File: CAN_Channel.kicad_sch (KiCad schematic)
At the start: 7 parts, among them J3 Conn_01x01, U2 TJA1051T-3

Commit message: LCD connector, backlight, other work
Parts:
- removed J3: Conn_01x01, Connector_PinHeader_2.54mm:PinHeader_1x01_P2.54mm_Vertical, symbol Connector_Generic:Conn_01x01
- removed S4: SLW-864587-2A-RA-N-D, SamacSys_Parts:SLW8645872ARAND, symbol SamacSys_Parts:SLW-864587-2A-RA-N-D
- added JP3: SolderJumper_2_Open, Jumper:SolderJumper-2_P1.3mm_Open_RoundedPad1.0x1.5mm, symbol Jumper:SolderJumper_2_Open
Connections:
- net CAN-: now also JP3.2 (B)
- net at R6.2: now also JP3.1 (A)
- no-connect marks 3 -> 0
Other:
- moved on the sheet: C15
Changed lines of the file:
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@@
 	(paper "A4")
 	(junction
-		(at 62.23 74.93)
+		(at 74.93 74.93)
 		(diameter 0)
 		(color 0 0 0 0)
@@
 		(color 0 0 0 0)
 	)
-	(no_connect
-		(at 180.34 76.2)
-	)
-	(no_connect
-		(at 180.34 66.04)
-	)
-	(no_connect
-		(at 180.34 68.58)
-	)
 	(wire
 		(pts
@@
 	(wire
 		(pts
-			(xy 62.23 74.93) (xy 93.98 74.93)
-		)
-		(stroke
-			(width 0)
-			(type default)
-		)
-	)
-	(wire
-		(pts
-			(xy 62.23 83.82) (xy 106.68 83.82)
-		)
-		(stroke
-			(width 0)
-			(type default)
-		)
-	)
-	(wire
-		(pts
-			(xy 62.23 74.93) (xy 62.23 72.39)
+			(xy 74.93 74.93) (xy 93.98 74.93)
+		)
+		(stroke
+			(width 0)
+			(type default)
+		)
+	)
+	(wire
+		(pts
+			(xy 74.93 83.82) (xy 106.68 83.82)
+		)
+		(stroke
+			(width 0)
+			(type default)
+		)
+	)
+	(wire
+		(pts
+			(xy 74.93 74.93) (xy 74.93 72.39)
 		)
 		(stroke
@@
 	(wire
 		(pts
-			(xy 62.23 82.55) (xy 62.23 83.82)
-		)
-		(stroke
-			(width 0)
-			(type default)
-		)
-	)
-	(wire
-		(pts
-			(xy 83.82 77.47) (xy 93.98 77.47)
+			(xy 74.93 82.55) (xy 74.93 83.82)
 		)
 		(stroke
@@
 	(hierarchical_label "CAN-"
 		(shape bidirectional)
-		(at 180.34 71.12 180)
+		(at 187.96 73.66 0)
 		(effects
 			(font
 				(size 1.27 1.27)
 			)
-			(justify right)
+			(justify left)
 		)
 	)
@@
 	)
 	(symbol
+		(lib_id "Jumper:SolderJumper_2_Open")
+		(at 184.15 73.66 0)
+		(unit 1)
+		(exclude_from_sim no)
+		(in_bom no)
+		(on_board yes)
+		(dnp no)
+		(fields_autoplaced yes)
+		(property "Reference" "JP3"
+			(at 184.15 67.31 0)
+			(effects
+				(font
+					(size 1.27 1.27)
+				)
+			)
+		)
+		(property "Value" "SolderJumper_2_Open"
+			(at 184.15 69.85 0)
+			(effects
+				(font
+					(size 1.27 1.27)
+				)
+			)
+		)
+		(property "Footprint" "Jumper:SolderJumper-2_P1.3mm_Open_RoundedPad1.0x1.5mm"
+			(at 184.15 73.66 0)
+			(effects
+				(font
+					(size 1.27 1.27)
+				)
+				(hide yes)
+			)
+		)
+		(property "Datasheet" "~"
+			(at 184.15 73.66 0)
+			(effects
+				(font
+					(size 1.27 1.27)
+				)
+				(hide yes)
+			)
+		)
+		(property "Description" "Solder Jumper, 2-pole, open"
+			(at 184.15 73.66 0)
+			(effects
+				(font
+					(size 1.27 1.27)
+				)
+				(hide yes)
+			)
+		)
+		(pin "2"
+		)
+		(pin "1"
+		)
+		(instances
+			(project "LV3-Dash"
+				(path "/f2bb7816-6b2a-47fd-8906-eb4aedd6f9e6/61479cd4-0d84-48d3-a2a5-35c815fbc6c8/26a5cdba-a2c0-4c6f-9b9d-6ff8cc92f2cc"
+					(reference "JP3")
+					(unit 1)
+				)
+			)
+		)
+	)
+	(symbol
 		(lib_id "power:+3.3V")
-		(at 62.23 72.39 0)
+		(at 74.93 72.39 0)
 		(unit 1)
 		(exclude_from_sim no)
@@
 		(fields_autoplaced yes)
 		(property "Reference" "#PWR019"
-			(at 62.23 76.2 0)
+			(at 74.93 76.2 0)
 			(effects
 				(font
@@
 		)
 		(property "Value" "+3.3V"
-			(at 62.23 67.31 0)
+			(at 74.93 67.31 0)
 			(effects
 				(font
@@
 		)
 		(property "Footprint" ""
-			(at 62.23 72.39 0)
+			(at 74.93 72.39 0)
 			(effects
 				(font
@@
 		)
 		(property "Datasheet" ""
-			(at 62.23 72.39 0)
+			(at 74.93 72.39 0)
 			(effects
 				(font
@@
 		)
 		(property "Description" "Power symbol creates a global label with name \"+3.3V\""
-			(at 62.23 72.39 0)
+			(at 74.93 72.39 0)
 			(effects
 				(font
@@
 	)
 	(symbol
-		(lib_id "Connector_Generic:Conn_01x01")
-		(at 78.74 77.47 180)
-		(unit 1)
-		(exclude_from_sim no)
-		(in_bom yes)
-		(on_board yes)
-		(dnp no)
-		(fields_autoplaced yes)
-		(property "Reference" "J3"
-			(at 78.74 71.12 0)
-			(effects
-				(font
-					(size 1.27 1.27)
-				)
-			)
-		)
-		(property "Value" "Conn_01x01"
-			(at 78.74 73.66 0)
-			(effects
-				(font
-					(size 1.27 1.27)
-				)
-			)
-		)
-		(property "Footprint" "Connector_PinHeader_2.54mm:PinHeader_1x01_P2.54mm_Vertical"
-			(at 78.74 77.47 0)
-			(effects
-				(font
-					(size 1.27 1.27)
-				)
-				(hide yes)
-			)
-		)
-		(property "Datasheet" "~"
-			(at 78.74 77.47 0)
-			(effects
-				(font
-					(size 1.27 1.27)
-				)
-				(hide yes)
-			)
-		)
-		(property "Description" "Generic connector, single row, 01x01, script generated (kicad-library-utils/schlib/autogen/connector/)"
-			(at 78.74 77.47 0)
-			(effects
-				(font
-					(size 1.27 1.27)
-				)
-				(hide yes)
-			)
-		)
-		(pin "1"
-		)
-		(instances
-			(project "LV3-Core"
-				(path "/f2bb7816-6b2a-47fd-8906-eb4aedd6f9e6/61479cd4-0d84-48d3-a2a5-35c815fbc6c8/26a5cdba-a2c0-4c6f-9b9d-6ff8cc92f2cc"
-					(reference "J3")
-					(unit 1)
-				)
-			)
-		)
-	)
-	(symbol
 		(lib_id "power:GND")
 		(at 106.68 83.82 0)
@@
 	(symbol
 		(lib_id "Device:C")
-		(at 62.23 78.74 0)
+		(at 74.93 78.74 0)
 		(unit 1)
 		(exclude_from_sim no)
@@
 		(fields_autoplaced yes)
 		(property "Reference" "C15"
-			(at 66.04 77.4699 0)
+			(at 78.74 77.4699 0)
 			(effects
 				(font
@@
 		)
 		(property "Value" "100n"
-			(at 66.04 80.0099 0)
+			(at 78.74 80.0099 0)
 			(effects
 				(font
@@
 		)
 		(property "Footprint" "Capacitor_SMD:C_0603_1608Metric_Pad1.08x0.95mm_HandSolder"
-			(at 63.1952 82.55 0)
+			(at 75.8952 82.55 0)
 			(effects
 				(font
@@
 		)
 		(property "Datasheet" "~"
-			(at 62.23 78.74 0)
+			(at 74.93 78.74 0)
 			(effects
 				(font
@@
 		)
 		(property "Description" "Unpolarized capacitor"
-			(at 62.23 78.74 0)
+			(at 74.93 78.74 0)
 			(effects
 				(font
@@
 					(unit 1)
 				)
-			)
-		)
-	)
-	(symbol
-		(lib_id "SamacSys_Parts:SLW-864587-2A-RA-N-D")
-		(at 180.34 66.04 0)
-		(unit 1)
-		(exclude_from_sim no)
-		(in_bom yes)
-		(on_board yes)
-		(dnp no)
-		(fields_autoplaced yes)
-		(property "Reference" "S4"
-			(at 199.39 69.8499 0)
-			(effects
-				(font
-					(size 1.27 1.27)
-				)
-				(justify left)
-			)
-		)
-		(property "Value" "SLW-864587-2A-RA-N-D"
-			(at 199.39 72.3899 0)
-			(effects
-				(font
-					(size 1.27 1.27)
-				)
-				(justify left)
-			)
-		)
-		(property "Footprint" "SamacSys_Parts:SLW8645872ARAND"
-			(at 199.39 160.96 0)
-			(effects
-				(font
-					(size 1.27 1.27)
-				)
-				(justify left top)
-				(hide yes)
-			)
-		)
-		(property "Datasheet" "https://www.sameskydevices.com/product/resource/slw-864587-2a-ra-n-d.pdf"
-			(at 199.39 260.96 0)
-			(effects
-				(font
-					(size 1.27 1.27)
-				)
-				(justify left top)
-				(hide yes)
-			)
-		)
-		(property "Description" "8.6 x 4.5 x 8.7 mm, 2 mm Raised Slide Actuator, Right Angle, Through Hole, Slide Switch"
-			(at 180.34 66.04 0)
-			(effects
-				(font
-					(size 1.27 1.27)
-				)
-				(hide yes)
-			)
-		)
-		(property "Height" "6.3"
-			(at 199.39 460.96 0)
-			(effects
-				(font
-					(size 1.27 1.27)
-				)
-				(justify left top)
-				(hide yes)
-			)
-		)
-		(property "Mouser Part Number" "179-SLW8645872ARAND"
-			(at 199.39 560.96 0)
-			(effects
-				(font
-					(size 1.27 1.27)
-				)
-				(justify left top)
-				(hide yes)
-			)
-		)
-		(property "Mouser Price/Stock" "https://www.mouser.co.uk/ProductDetail/Same-Sky/SLW-864587-2A-RA-N-D?qs=IKkN%2F947nfDwxE1B2lS5tw%3D%3D"
-			(at 199.39 660.96 0)
-			(effects
-				(font
-					(size 1.27 1.27)
-				)
-				(justify left top)
-				(hide yes)
-			)
-		)
-		(property "Manufacturer_Name" "Same Sky"
-			(at 199.39 760.96 0)
-			(effects
-				(font
-					(size 1.27 1.27)
-				)
-				(justify left top)
-				(hide yes)
-			)
-		)
-		(property "Manufacturer_Part_Number" "SLW-864587-2A-RA-N-D"
-			(at 199.39 860.96 0)
-			(effects
-				(font
-					(size 1.27 1.27)
-				)
-				(justify left top)
-				(hide yes)
-			)
-		)
-		(pin "2"
-		)
-		(pin "4"
-		)
-		(pin "5"
-		)
-		(pin "1"
-		)
-		(pin "3"
-		)
-		(instances
-			(project "LV3-Core"
-				(path "/f2bb7816-6b2a-47fd-8906-eb4aedd6f9e6/61479cd4-0d84-48d3-a2a5-35c815fbc6c8/26a5cdba-a2c0-4c6f-9b9d-6ff8cc92f2cc"
-					(reference "S4")
-					(unit 1)
-				)

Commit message: preliminary complete schematic
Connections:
- net GND: now also U2.8 (S)
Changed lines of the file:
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@@
+	)
+	(junction
+		(at 90.17 83.82)
+		(diameter 0)
+		(color 0 0 0 0)
 	)
 	(junction
@@
 		(pts
 			(xy 165.1 73.66) (xy 162.56 73.66)
+		)
+		(stroke
+			(width 0)
+			(type default)
+		)
+	)
+	(wire
+		(pts
+			(xy 90.17 77.47) (xy 90.17 83.82)
+		)
+		(stroke
+			(width 0)
+			(type default)
+		)
+	)
+	(wire
+		(pts
+			(xy 93.98 77.47) (xy 90.17 77.47)
+		)
+		(stroke
+			(width 0)
+			(type default)
+		)
+	)
+	(wire
+		(pts
+			(xy 90.17 83.82) (xy 106.68 83.82)
 		)
 		(stroke
@@
 	(wire
 		(pts
-			(xy 74.93 83.82) (xy 106.68 83.82)
+			(xy 74.93 83.82) (xy 90.17 83.82)
 		)
 		(stroke

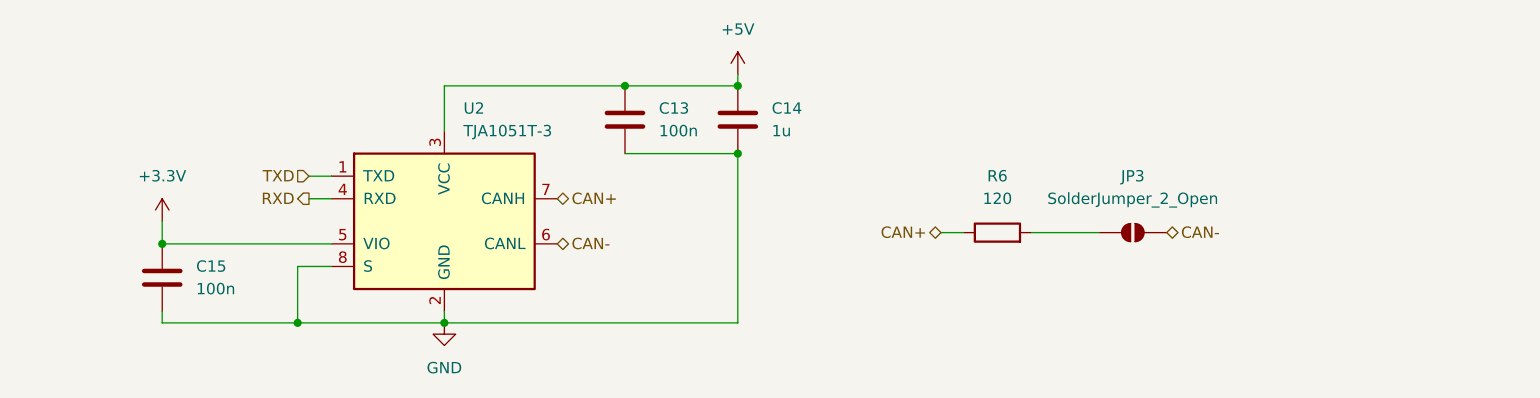
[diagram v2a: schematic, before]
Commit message: basic layout organization, fix +VDDA typo
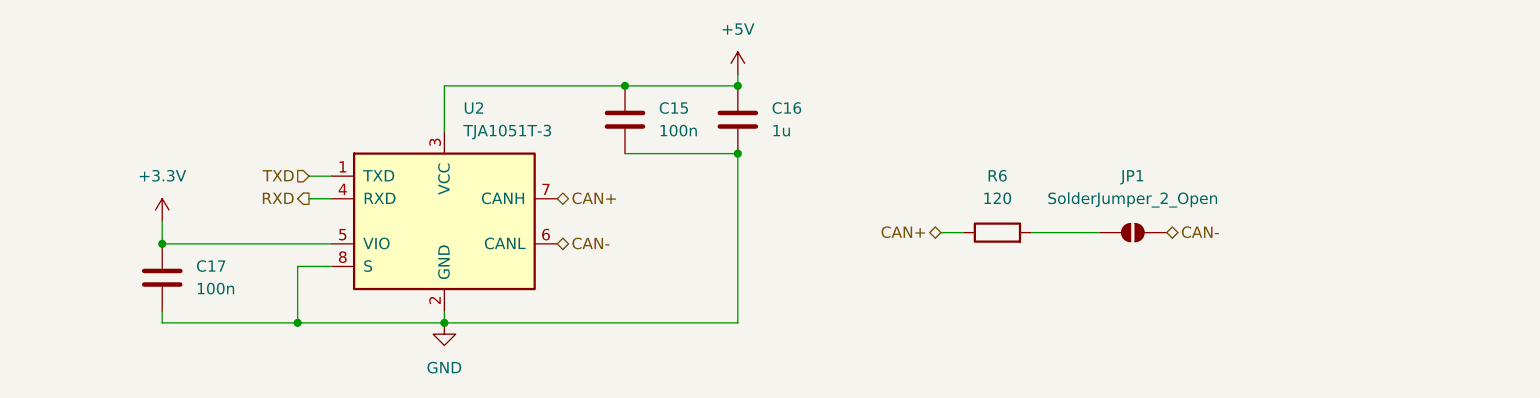
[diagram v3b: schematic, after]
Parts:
- renumbered C13 to C15, C14 to C16, C15 to C17, JP3 to JP1
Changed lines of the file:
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@@
 		(dnp no)
 		(fields_autoplaced yes)
-		(property "Reference" "JP3"
+		(property "Reference" "JP1"
 			(at 184.15 67.31 0)
 			(effects
@@
 			(project "LV3-Dash"
 				(path "/f2bb7816-6b2a-47fd-8906-eb4aedd6f9e6/61479cd4-0d84-48d3-a2a5-35c815fbc6c8/26a5cdba-a2c0-4c6f-9b9d-6ff8cc92f2cc"
-					(reference "JP3")
+					(reference "JP1")
 					(unit 1)
 				)
@@
 		(dnp no)
 		(fields_autoplaced yes)
-		(property "Reference" "#PWR019"
+		(property "Reference" "#PWR020"
 			(at 74.93 76.2 0)
 			(effects
@@
 			(project "LV3-Core"
 				(path "/f2bb7816-6b2a-47fd-8906-eb4aedd6f9e6/61479cd4-0d84-48d3-a2a5-35c815fbc6c8/26a5cdba-a2c0-4c6f-9b9d-6ff8cc92f2cc"
-					(reference "#PWR019")
+					(reference "#PWR020")
 					(unit 1)
 				)
@@
 		(dnp no)
 		(fields_autoplaced yes)
-		(property "Reference" "#PWR018"
+		(property "Reference" "#PWR019"
 			(at 139.7 59.69 0)
 			(effects
@@
 			(project "LV3-Core"
 				(path "/f2bb7816-6b2a-47fd-8906-eb4aedd6f9e6/61479cd4-0d84-48d3-a2a5-35c815fbc6c8/26a5cdba-a2c0-4c6f-9b9d-6ff8cc92f2cc"
-					(reference "#PWR018")
+					(reference "#PWR019")
 					(unit 1)
 				)
@@
 		(dnp no)
 		(fields_autoplaced yes)
-		(property "Reference" "C13"
+		(property "Reference" "C15"
 			(at 130.81 59.6899 0)
 			(effects
@@
 			(project "LV3-Core"
 				(path "/f2bb7816-6b2a-47fd-8906-eb4aedd6f9e6/61479cd4-0d84-48d3-a2a5-35c815fbc6c8/26a5cdba-a2c0-4c6f-9b9d-6ff8cc92f2cc"
-					(reference "C13")
+					(reference "C15")
 					(unit 1)
 				)
@@
 		(dnp no)
 		(fields_autoplaced yes)
-		(property "Reference" "C14"
+		(property "Reference" "C16"
 			(at 143.51 59.6899 0)
 			(effects
@@
 			(project "LV3-Core"
 				(path "/f2bb7816-6b2a-47fd-8906-eb4aedd6f9e6/61479cd4-0d84-48d3-a2a5-35c815fbc6c8/26a5cdba-a2c0-4c6f-9b9d-6ff8cc92f2cc"
-					(reference "C14")
+					(reference "C16")
 					(unit 1)
 				)
@@
 		(dnp no)
 		(fields_autoplaced yes)
-		(property "Reference" "#PWR020"
+		(property "Reference" "#PWR021"
 			(at 106.68 90.17 0)
 			(effects
@@
 			(project "LV3-Core"
 				(path "/f2bb7816-6b2a-47fd-8906-eb4aedd6f9e6/61479cd4-0d84-48d3-a2a5-35c815fbc6c8/26a5cdba-a2c0-4c6f-9b9d-6ff8cc92f2cc"
-					(reference "#PWR020")
+					(reference "#PWR021")
 					(unit 1)
 				)
@@
 		(dnp no)
 		(fields_autoplaced yes)
-		(property "Reference" "C15"
+		(property "Reference" "C17"
 			(at 78.74 77.4699 0)
 			(effects
@@
 			(project "LV3-Core"
 				(path "/f2bb7816-6b2a-47fd-8906-eb4aedd6f9e6/61479cd4-0d84-48d3-a2a5-35c815fbc6c8/26a5cdba-a2c0-4c6f-9b9d-6ff8cc92f2cc"
-					(reference "C15")
-					(unit 1)
-				)
+					(reference "C17")
+					(unit 1)
+				)
